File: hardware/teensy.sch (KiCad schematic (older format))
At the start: 26 parts, among them P5 USB_OTG, SW1 SW_PUSH, U2 LP38691, U3 MKL02Z32, U4 MK20DX256VLH7, Y1 16 MHz, Y2 32.768 kHz

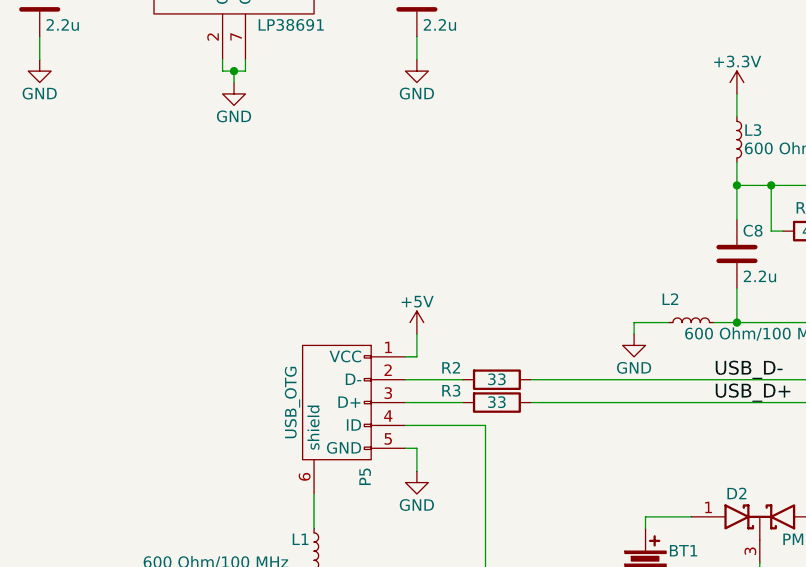
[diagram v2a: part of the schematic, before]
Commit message: Added DC jack for 5V input.  Updated layout
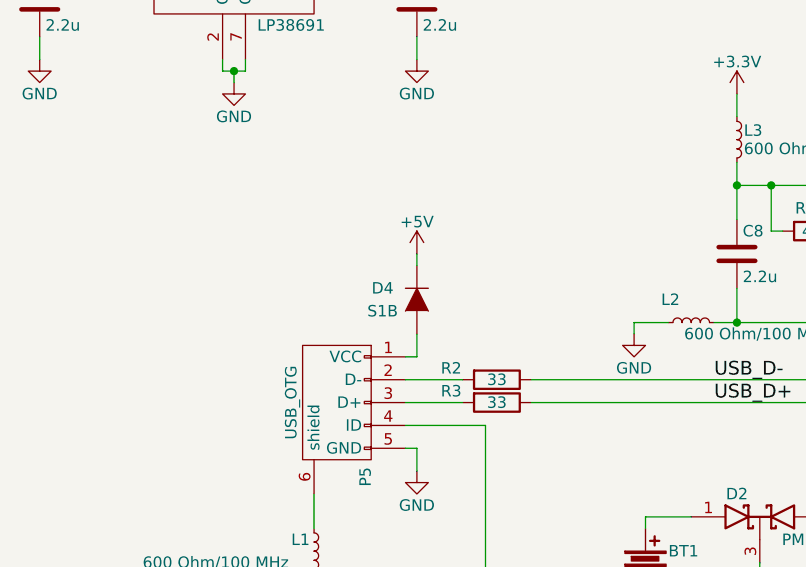
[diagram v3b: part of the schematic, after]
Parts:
- added D4: S1B, Diodes_SMD:SMA_Standard, symbol D
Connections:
- net +5V: now also D4.1 (K); no longer P5.1 (VCC)
- new net: D4.2 (A), P5.1 (VCC)
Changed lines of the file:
@@
 $EndComp
 $Comp
-L GND #PWR038
+L GND #PWR042
 U 1 1 57630FB2
 P 3550 5700
-F 0 "#PWR038" H 3550 5450 50  0001 C CNN
+F 0 "#PWR042" H 3550 5450 50  0001 C CNN
 F 1 "GND" H 3550 5550 50  0000 C CNN
 F 2 "" H 3550 5700 50  0000 C CNN
@@
 $EndComp
 $Comp
-L +3.3V #PWR039
+L +3.3V #PWR043
 U 1 1 57630FBC
 P 3550 4700
-F 0 "#PWR039" H 3550 4550 50  0001 C CNN
+F 0 "#PWR043" H 3550 4550 50  0001 C CNN
 F 1 "+3.3V" H 3550 4840 50  0000 C CNN
 F 2 "" H 3550 4700 50  0000 C CNN
@@
 $EndComp
 $Comp
-L GND #PWR040
+L GND #PWR044
 U 1 1 57630FC2
 P 5800 6000
-F 0 "#PWR040" H 5800 5750 50  0001 C CNN
+F 0 "#PWR044" H 5800 5750 50  0001 C CNN
 F 1 "GND" H 5800 5850 50  0000 C CNN
 F 2 "" H 5800 6000 50  0000 C CNN
@@
 $EndComp
 $Comp
-L GND #PWR041
+L GND #PWR045
 U 1 1 57630FD0
 P 3150 6000
-F 0 "#PWR041" H 3150 5750 50  0001 C CNN
+F 0 "#PWR045" H 3150 5750 50  0001 C CNN
 F 1 "GND" H 3150 5850 50  0000 C CNN
 F 2 "" H 3150 6000 50  0000 C CNN
@@
 NoConn ~ 4900 5400
 $Comp
-L +3.3V #PWR042
+L +3.3V #PWR046
 U 1 1 57630FE2
 P 5750 1200
-F 0 "#PWR042" H 5750 1050 50  0001 C CNN
+F 0 "#PWR046" H 5750 1050 50  0001 C CNN
 F 1 "+3.3V" H 5750 1340 50  0000 C CNN
 F 2 "" H 5750 1200 50  0000 C CNN
@@
 $EndComp
 $Comp
-L GND #PWR043
+L GND #PWR047
 U 1 1 57631016
 P 2000 5450
-F 0 "#PWR043" H 2000 5200 50  0001 C CNN
+F 0 "#PWR047" H 2000 5200 50  0001 C CNN
 F 1 "GND" H 2000 5300 50  0000 C CNN
 F 2 "" H 2000 5450 50  0000 C CNN
@@
 $EndComp
 $Comp
-L +3.3V #PWR044
+L +3.3V #PWR048
 U 1 1 5763101C
 P 2000 5050
-F 0 "#PWR044" H 2000 4900 50  0001 C CNN
+F 0 "#PWR048" H 2000 4900 50  0001 C CNN
 F 1 "+3.3V" H 2000 5190 50  0000 C CNN
 F 2 "" H 2000 5050 50  0000 C CNN
@@
 $EndComp
 $Comp
-L GND #PWR045
+L GND #PWR049
 U 1 1 5763102B
 P 4100 4050
-F 0 "#PWR045" H 4100 3800 50  0001 C CNN
+F 0 "#PWR049" H 4100 3800 50  0001 C CNN
 F 1 "GND" H 4100 3900 50  0000 C CNN
 F 2 "" H 4100 4050 50  0000 C CNN
@@
 $EndComp
 $Comp
-L GND #PWR046
+L GND #PWR050
 U 1 1 57631066
 P 4050 2850
-F 0 "#PWR046" H 4050 2600 50  0001 C CNN
+F 0 "#PWR050" H 4050 2600 50  0001 C CNN
 F 1 "GND" H 4050 2700 50  0000 C CNN
 F 2 "" H 4050 2850 50  0000 C CNN
@@
 $EndComp
 $Comp
-L +3.3V #PWR047
+L +3.3V #PWR051
 U 1 1 57631075
 P 4500 1800
-F 0 "#PWR047" H 4500 1650 50  0001 C CNN
+F 0 "#PWR051" H 4500 1650 50  0001 C CNN
 F 1 "+3.3V" H 4500 1940 50  0000 C CNN
 F 2 "" H 4500 1800 50  0000 C CNN
@@
 $EndComp
 $Comp
-L +3.3V #PWR048
+L +3.3V #PWR052
 U 1 1 57631098
 P 9650 1000
-F 0 "#PWR048" H 9650 850 50  0001 C CNN
+F 0 "#PWR052" H 9650 850 50  0001 C CNN
 F 1 "+3.3V" H 9650 1140 50  0000 C CNN
 F 2 "" H 9650 1000 50  0000 C CNN
@@
 $EndComp
 $Comp
-L GND #PWR049
+L GND #PWR053
 U 1 1 5763109E
 P 9650 1500
-F 0 "#PWR049" H 9650 1250 50  0001 C CNN
+F 0 "#PWR053" H 9650 1250 50  0001 C CNN
 F 1 "GND" H 9650 1350 50  0000 C CNN
 F 2 "" H 9650 1500 50  0000 C CNN
@@
 $EndComp
 $Comp
-L GND #PWR050
+L GND #PWR054
 U 1 1 57632880
 P 2650 3950
-F 0 "#PWR050" H 2650 3700 50  0001 C CNN
+F 0 "#PWR054" H 2650 3700 50  0001 C CNN
 F 1 "GND" H 2650 3800 50  0000 C CNN
 F 2 "" H 2650 3950 50  0000 C CNN
@@
 $EndComp
 $Comp
-L GND #PWR051
+L GND #PWR055
 U 1 1 576328C7
 P 3100 3450
-F 0 "#PWR051" H 3100 3200 50  0001 C CNN
+F 0 "#PWR055" H 3100 3200 50  0001 C CNN
 F 1 "GND" H 3100 3300 50  0000 C CNN
 F 2 "" H 3100 3450 50  0000 C CNN
@@
 $EndComp
 $Comp
-L +5V #PWR052
+L +5V #PWR056
 U 1 1 5763FF76
-P 3100 2850
-F 0 "#PWR052" H 3100 2700 50  0001 C CNN
-F 1 "+5V" H 3100 2990 50  0000 C CNN
-F 2 "" H 3100 2850 50  0000 C CNN
-F 3 "" H 3100 2850 50  0000 C CNN
-	1    3100 2850
+P 3100 2500
+F 0 "#PWR056" H 3100 2350 50  0001 C CNN
+F 1 "+5V" H 3100 2640 50  0000 C CNN
+F 2 "" H 3100 2500 50  0000 C CNN
+F 3 "" H 3100 2500 50  0000 C CNN
+	1    3100 2500
 	1    0    0    -1
 $EndComp
@@
 $EndComp
 $Comp
-L +5V #PWR053
+L +5V #PWR057
 U 1 1 57640ACB
 P 1450 1050
-F 0 "#PWR053" H 1450 900 50  0001 C CNN
+F 0 "#PWR057" H 1450 900 50  0001 C CNN
 F 1 "+5V" H 1450 1190 50  0000 C CNN
 F 2 "" H 1450 1050 50  0000 C CNN
@@
 $EndComp
 $Comp
-L +3.3V #PWR054
+L +3.3V #PWR058
 U 1 1 57641034
 P 3100 1050
-F 0 "#PWR054" H 3100 900 50  0001 C CNN
+F 0 "#PWR058" H 3100 900 50  0001 C CNN
 F 1 "+3.3V" H 3100 1190 50  0000 C CNN
 F 2 "" H 3100 1050 50  0000 C CNN
@@
 $EndComp
 $Comp
-L GND #PWR055
+L GND #PWR059
 U 1 1 57641148
 P 3100 1650
-F 0 "#PWR055" H 3100 1400 50  0001 C CNN
+F 0 "#PWR059" H 3100 1400 50  0001 C CNN
 F 1 "GND" H 3100 1500 50  0000 C CNN
 F 2 "" H 3100 1650 50  0000 C CNN
@@
 $EndComp
 $Comp
-L GND #PWR056
+L GND #PWR060
 U 1 1 5764119E
 P 1450 1650
-F 0 "#PWR056" H 1450 1400 50  0001 C CNN
+F 0 "#PWR060" H 1450 1400 50  0001 C CNN
 F 1 "GND" H 1450 1500 50  0000 C CNN
 F 2 "" H 1450 1650 50  0000 C CNN
@@
 $EndComp
 $Comp
-L GND #PWR057
+L GND #PWR061
 U 1 1 576416D5
 P 2300 1750
-F 0 "#PWR057" H 2300 1500 50  0001 C CNN
+F 0 "#PWR061" H 2300 1500 50  0001 C CNN
 F 1 "GND" H 2300 1600 50  0000 C CNN
 F 2 "" H 2300 1750 50  0000 C CNN
@@
 	1700 1250 1700 1150
 Connection ~ 1700 1150
-Wire Wire Line
-	3100 2950 3050 2950
-Wire Wire Line
-	3100 2850 3100 2950
 $Comp
 L L_Small L1
@@
 $EndComp
 $Comp
-L GND #PWR058
+L GND #PWR062
 U 1 1 57671E49
 P 5700 4600
-F 0 "#PWR058" H 5700 4350 50  0001 C CNN
+F 0 "#PWR062" H 5700 4350 50  0001 C CNN
 F 1 "GND" H 5700 4450 50  0000 C CNN
 F 2 "" H 5700 4600 50  0000 C CNN
@@
 	4100 4050 4100 4000
 $Comp
-L +3.3V #PWR059
+L +3.3V #PWR063
 U 1 1 576736EE
 P 4950 3550
-F 0 "#PWR059" H 4950 3400 50  0001 C CNN
+F 0 "#PWR063" H 4950 3400 50  0001 C CNN
 F 1 "+3.3V" H 4950 3690 50  0000 C CNN
 F 2 "" H 4950 3550 50  0000 C CNN
@@
 Text Label 4400 3150 0    60   ~ 0
 USB_D+
+$Comp
+L D D4
+U 1 1 577ED6C5
+P 3100 2700
+F 0 "D4" V 3050 2550 50  0000 C CNN
+F 1 "S1B" V 3150 2550 50  0000 C CNN
+F 2 "Diodes_SMD:SMA_Standard" H 3100 2700 50  0001 C CNN
+F 3 "" H 3100 2700 50  0000 C CNN
+	1    3100 2700
+	0    1    1    0
+$EndComp
+Wire Wire Line
+	3100 2950 3050 2950
+Wire Wire Line
+	3100 2550 3100 2500
+Wire Wire Line
+	3100 2950 3100 2850
 $EndSCHEMATC
